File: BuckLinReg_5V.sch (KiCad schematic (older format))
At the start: 71 parts, among them J1 Barrel_Jack, J2 796638-4, J3 1x2 Male, J4 796634-4, Q1 PMBT2222, Q2 SQD40061EL, SW1 SW_SPDT, U1 TLV76050DBZT, U2 LMV358, U3 74HCT00, U4 SN74HCT02, U5 TCM810, U6 TPS56339DDC, U7 LM1084-5.0

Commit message: PCB Ordered
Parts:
- removed Q2: SQD40061EL, Package_TO_SOT_SMD:TO-252-2, symbol Device:Q_PMOS_GDS
- removed TP14: ~Q, TestPoint:TestPoint_THTPad_D2.0mm_Drill1.0mm, symbol Connector:TestPoint
- removed TP8: ~PWR_EN, TestPoint:TestPoint_THTPad_D2.0mm_Drill1.0mm, symbol Connector:TestPoint
- added Q2: Si4435FDY, Package_SO:SO-8_3.9x4.9mm_P1.27mm, symbol BuckLinReg_5V:Si4435FDY
- C2, C3: MFPN CGA5L1X7R1H106K160AE -> C3216X7R1H106K160AC
- C8, C9: MFPN CL32B106KBJNNNE -> ‎CL32B106KBJNNWE‎
- J2: MFPN (none) -> 796638-4
- J4: MFPN (none) -> 796634-4
- U7: value LM1084-5.0 -> LM1085ISX-5.0/NOPB; MFPN LM1084ISX-5.0/NOPB -> LM1085ISX-5.0/NOPB
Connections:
- net +Vin: now also C9.1, Q2.1 (S), Q2.2 (S), Q2.3 (S); no longer C3.1
- net PCheckG: now also Q2.4 (G)
- net SR+: now also C3.1; no longer C9.1
- net Vin: now also Q2.5 (D), Q2.6 (D), Q2.7 (D), Q2.8 (D)
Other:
- moved on the sheet: C3, C9
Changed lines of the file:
@@
 	9225 4150 9425 4150
-Wire Wire Line
-	3275 4825 3200 4825
 Wire Wire Line
 	3575 4825 3625 4825
@@
 Wire Wire Line
 	8000 7825 7950 7825
-Wire Wire Line
-	8000 7350 8000 7650
 Wire Wire Line
 	7950 7350 8000 7350
@@
 $EndComp
 $Comp
-L Device:Q_PMOS_GDS Q2
-U 1 1 602222D6
-P 5875 2050
-F 0 "Q2" V 6217 2050 50  0000 C CNN
-F 1 "SQD40061EL" V 6126 2050 50  0000 C CNN
-F 2 "Package_TO_SOT_SMD:TO-252-2" H 6075 2150 50  0001 C CNN
-F 3 "~" H 5875 2050 50  0001 C CNN
-F 4 "SQD40061EL" H 5875 2050 50  0001 C CNN "MFPN"
-	1    5875 2050
-	0    -1   -1   0
-$EndComp
-$Comp
 L Connector:Barrel_Jack J1
 U 1 1 602194BD
@@
 L Device:C_Small C9
 U 1 1 601E51F0
-P 8350 4400
-F 0 "C9" H 8442 4446 50  0000 L CNN
-F 1 "10u" H 8442 4355 50  0000 L CNN
-F 2 "Capacitor_SMD:C_1210_3225Metric_Pad1.33x2.70mm_HandSolder" H 8350 4400 50  0001 C CNN
-F 3 "~" H 8350 4400 50  0001 C CNN
-F 4 "CL32B106KBJNNNE" H 8350 4400 50  0001 C CNN "MFPN"
-	1    8350 4400
+P 2075 4400
+F 0 "C9" H 2167 4446 50  0000 L CNN
+F 1 "10u" H 2167 4355 50  0000 L CNN
+F 2 "Capacitor_SMD:C_1210_3225Metric_Pad1.33x2.70mm_HandSolder" H 2075 4400 50  0001 C CNN
+F 3 "~" H 2075 4400 50  0001 C CNN
+F 4 "‎CL32B106KBJNNWE‎" H 2075 4400 50  0001 C CNN "MFPN"
+	1    2075 4400
 	1    0    0    -1
 $EndComp
@@
 F 2 "Capacitor_SMD:C_1210_3225Metric_Pad1.33x2.70mm_HandSolder" H 8025 4400 50  0001 C CNN
 F 3 "~" H 8025 4400 50  0001 C CNN
-F 4 "CL32B106KBJNNNE" H 8025 4400 50  0001 C CNN "MFPN"
+F 4 "‎CL32B106KBJNNWE‎" H 8025 4400 50  0001 C CNN "MFPN"
 	1    8025 4400
 	1    0    0    -1
@@
 L Device:C_Small C3
 U 1 1 601DCCF3
-P 2075 4400
-F 0 "C3" H 2167 4446 50  0000 L CNN
-F 1 "10u" H 2167 4355 50  0000 L CNN
-F 2 "Capacitor_SMD:C_1206_3216Metric_Pad1.33x1.80mm_HandSolder" H 2075 4400 50  0001 C CNN
-F 3 "~" H 2075 4400 50  0001 C CNN
-F 4 "CGA5L1X7R1H106K160AE" H 2075 4400 50  0001 C CNN "MFPN"
-	1    2075 4400
+P 8350 4400
+F 0 "C3" H 8442 4446 50  0000 L CNN
+F 1 "10u" H 8442 4355 50  0000 L CNN
+F 2 "Capacitor_SMD:C_1206_3216Metric_Pad1.33x1.80mm_HandSolder" H 8350 4400 50  0001 C CNN
+F 3 "~" H 8350 4400 50  0001 C CNN
+F 4 "C3216X7R1H106K160AC" H 8350 4400 50  0001 C CNN "MFPN"
+	1    8350 4400
 	1    0    0    -1
 $EndComp
@@
 F 2 "Capacitor_SMD:C_1206_3216Metric_Pad1.33x1.80mm_HandSolder" H 1750 4400 50  0001 C CNN
 F 3 "~" H 1750 4400 50  0001 C CNN
-F 4 "CGA5L1X7R1H106K160AE" H 1750 4400 50  0001 C CNN "MFPN"
+F 4 "C3216X7R1H106K160AC" H 1750 4400 50  0001 C CNN "MFPN"
 	1    1750 4400
 	1    0    0    -1
@@
 P 10500 4150
 F 0 "U7" H 10500 4392 50  0000 C CNN
-F 1 "LM1084-5.0" H 10500 4301 50  0000 C CNN
+F 1 "LM1085ISX-5.0/NOPB" H 10500 4301 50  0000 C CNN
 F 2 "Package_TO_SOT_SMD:TO-263-3_TabPin2" H 10500 4400 50  0001 C CIN
 F 3 "http://www.ti.com/general/docs/suppproductinfo.tsp?distId=10&gotoUrl=http%3A%2F%2Fwww.ti.com%2Flit%2Fgpn%2Flm1084" H 10500 4150 50  0001 C CNN
-F 4 "LM1084ISX-5.0/NOPB" H 10500 4150 50  0001 C CNN "MFPN"
+F 4 "LM1085ISX-5.0/NOPB" H 10500 4150 50  0001 C CNN "MFPN"
 	1    10500 4150
 	1    0    0    -1
@@
 Connection ~ 7375 8875
 $Comp
-L Connector:TestPoint TP14
-U 1 1 604CB1A8
-P 8050 7650
-F 0 "TP14" H 8108 7768 50  0000 L CNN
-F 1 "~Q" H 8108 7677 50  0000 L CNN
-F 2 "TestPoint:TestPoint_THTPad_D2.0mm_Drill1.0mm" H 8250 7650 50  0001 C CNN
-F 3 "~" H 8250 7650 50  0001 C CNN
-	1    8050 7650
-	0    1    -1   0
-$EndComp
-Wire Wire Line
-	8050 7650 8000 7650
-Connection ~ 8000 7650
-Wire Wire Line
-	8000 7650 8000 7825
-$Comp
 L Connector:TestPoint TP12
 U 1 1 604EEC3C
@@
 	7300 7250 7300 7150
 $Comp
-L Connector:TestPoint TP8
-U 1 1 605351DA
-P 3200 4700
-F 0 "TP8" H 3258 4818 50  0000 L CNN
-F 1 "~PWR_EN" H 3258 4727 50  0000 L CNN
-F 2 "TestPoint:TestPoint_THTPad_D2.0mm_Drill1.0mm" H 3400 4700 50  0001 C CNN
-F 3 "~" H 3400 4700 50  0001 C CNN
-	1    3200 4700
-	-1   0    0    -1
-$EndComp
-Wire Wire Line
-	3200 4700 3200 4825
-Connection ~ 3200 4825
-Wire Wire Line
-	3200 4825 3125 4825
-$Comp
 L Connector:TestPoint TP15
 U 1 1 6056A5D9
@@
 F 2 "BuckLinReg_5V:796636-4" H 11500 4150 50  0001 C CNN
 F 3 "~" H 11500 4150 50  0001 C CNN
+F 4 "796638-4" H 11500 4150 50  0001 C CNN "MFPN"
 	1    11500 4150
 	1    0    0    -1
@@
 F 2 "" H 12275 4150 50  0001 C CNN
 F 3 "~" H 12275 4150 50  0001 C CNN
+F 4 "796634-4" H 12275 4150 50  0001 C CNN "MFPN"
 	1    12275 4150
 	1    0    0    -1
@@
 Text Notes 12500 4125 0    50   ~ 0
 Included to be present\non the BOM table
+Wire Wire Line
+	3125 4825 3275 4825
+Wire Wire Line
+	8000 7350 8000 7825
+$Comp
+L BuckLinReg_5V:Si4435FDY Q2
+U 1 1 6059001A
+P 5875 2000
+F 0 "Q2" V 6167 2000 50  0000 C CNN
+F 1 "Si4435FDY" V 6076 2000 50  0000 C CNN
+F 2 "Package_SO:SO-8_3.9x4.9mm_P1.27mm" H 5875 2450 50  0001 C CNN
+F 3 "" H 5875 2450 50  0001 C CNN
+	1    5875 2000
+	0    -1   -1   0
+$EndComp
 $EndSCHEMATC

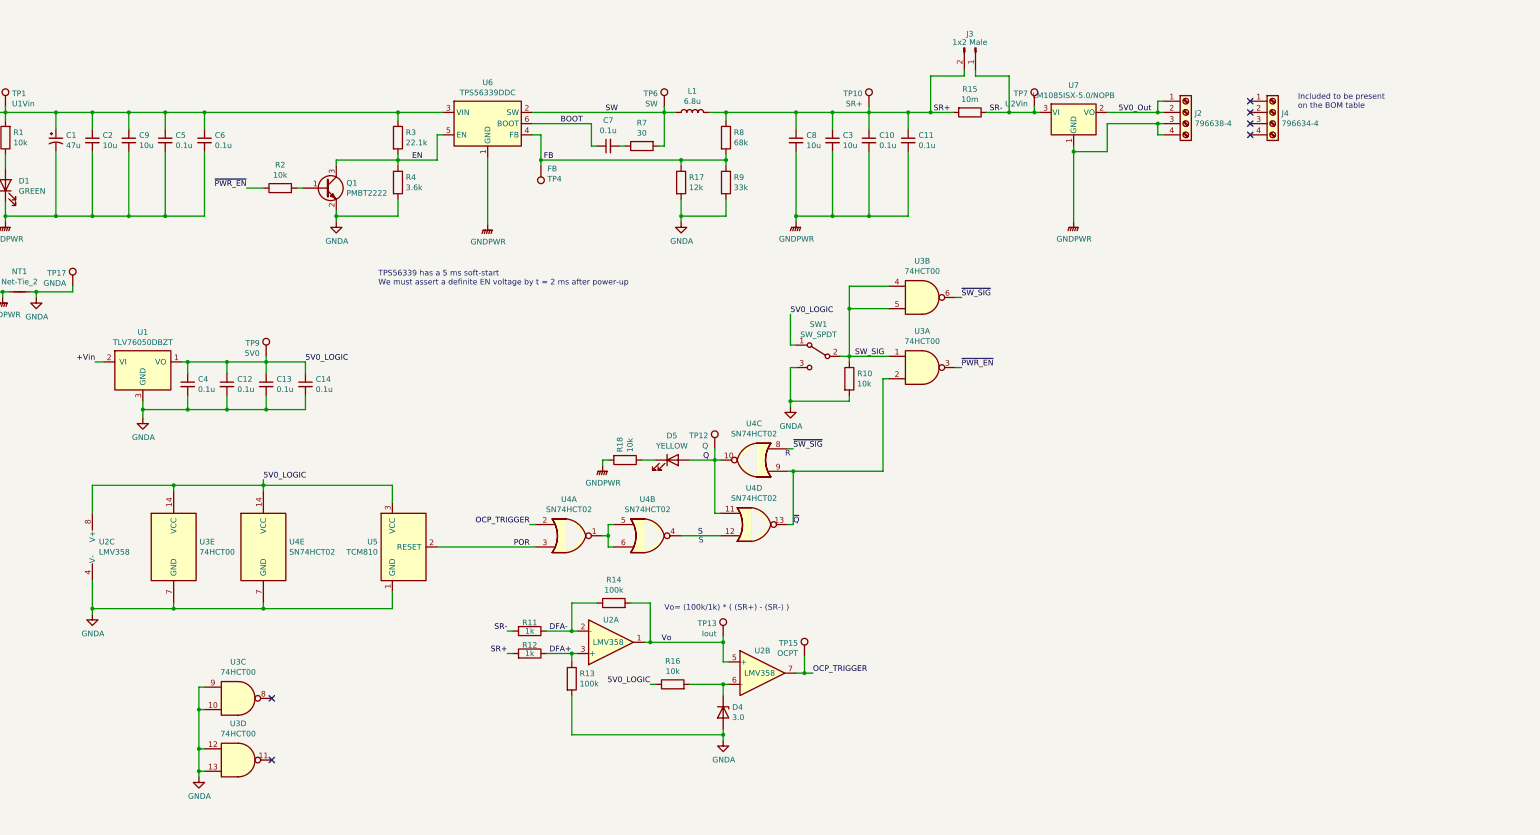
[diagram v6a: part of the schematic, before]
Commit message: Begin rev. 2 sch and PCB resize to 94x54mm
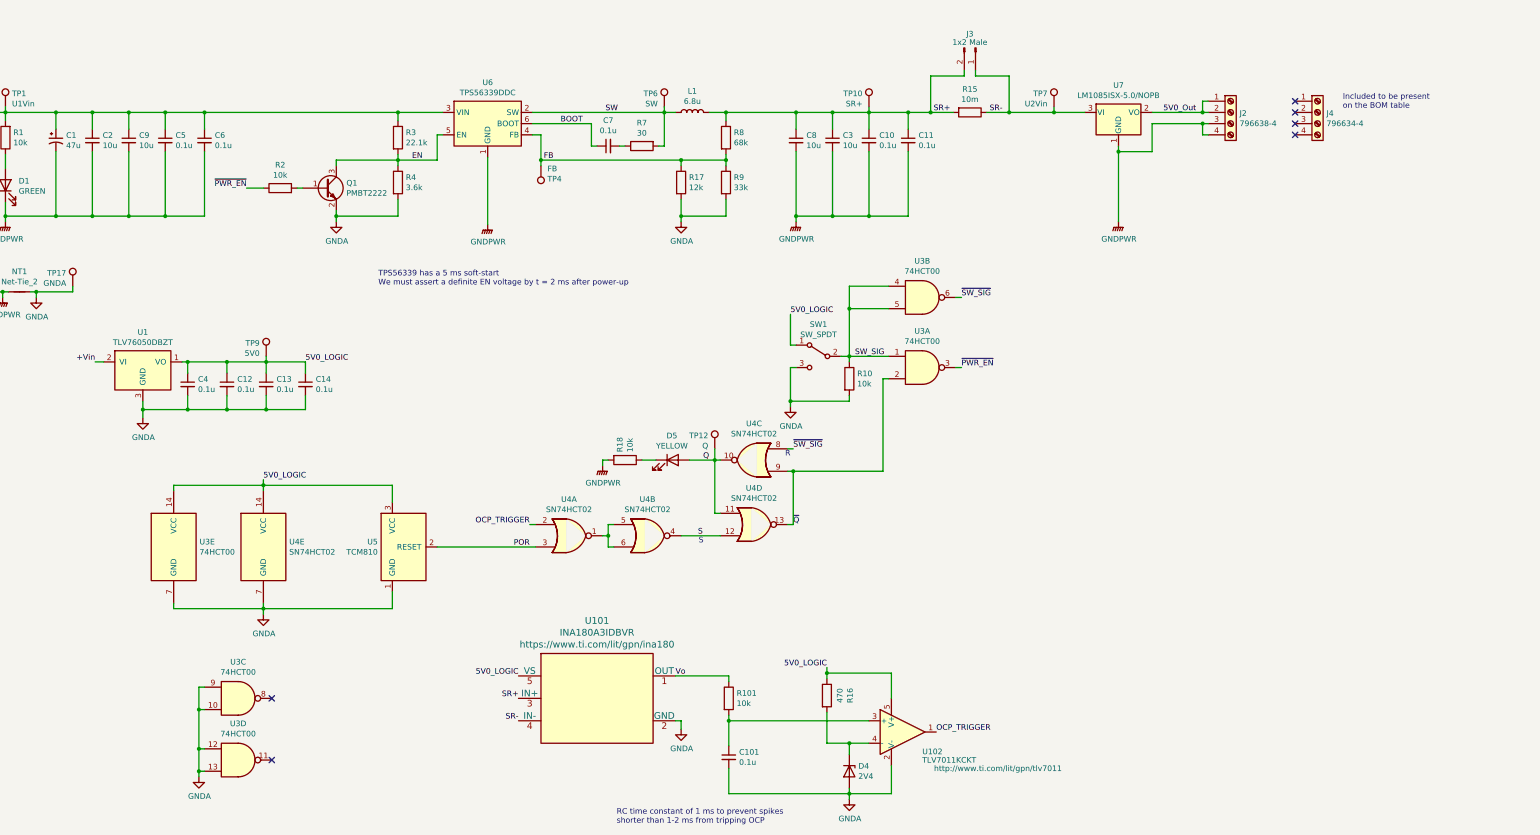
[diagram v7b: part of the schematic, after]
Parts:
- removed R11, R12: 1k, Resistor_SMD:R_1206_3216Metric_Pad1.30x1.75mm_HandSolder, symbol Device:R
- removed R13, R14: 100k, Resistor_SMD:R_1206_3216Metric_Pad1.30x1.75mm_HandSolder, symbol Device:R
- removed TP13: Iout, TestPoint:TestPoint_THTPad_D2.0mm_Drill1.0mm, symbol Connector:TestPoint
- removed TP15: OCPT, TestPoint:TestPoint_THTPad_D2.0mm_Drill1.0mm, symbol Connector:TestPoint
- removed U2: LMV358, Package_SO:SOIC-8_3.9x4.9mm_P1.27mm, symbol Amplifier_Operational:LMV358
- added C101: 0.1u, Capacitor_SMD:C_0603_1608Metric_Pad1.08x0.95mm_HandSolder, symbol Device:C_Small
- added R101: 10k, Resistor_SMD:R_1206_3216Metric_Pad1.30x1.75mm_HandSolder, symbol Device:R
- added U101: INA180A3IDBVR, Package_TO_SOT_SMD:SOT-23-5_HandSoldering, symbol BuckLinReg_5V:INA180A3IDBVR
- added U102: TLV7011KCKT, Package_TO_SOT_SMD:SOT-23-5_HandSoldering, symbol Comparator:TLV7031DBV
- D4: value 3.0 -> 2V4; footprint Diode_SMD:D_SOD-323 -> Package_TO_SOT_SMD:SOT-23_Handsoldering; MFPN PDZ3.0B,115 -> BZX84-C2V4,215
- R16: value 10k -> 470
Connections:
- net 5V0_LOGIC: now also U101.5 (VS), U102.5 (V+)
- net GNDA: now also C101.2, U101.2 (GND), U102.2 (V-)
- net OCP_TRIGGER: now also U102.1
- net SR+: now also U101.3 (IN+)
- net SR-: now also U101.4 (IN-)
- net Vo: now also R101.1, U101.1 (OUT)
- net at D4.1 (K), R16.2: now also U102.4 (-)
- new net: C101.1, R101.2, U102.3 (+)
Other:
- note added: "RC time constant of 1 ms to prevent spikes\nshorter than 1-2 ms from tripping OCP"
- note removed: "Vo= (100k/1k) * ( (SR+) - (SR-) )"
- moved on the sheet: D4, J2, J4, R16, TP7, U7

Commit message: Completed initial layout of rev. 2
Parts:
- D4: footprint Package_TO_SOT_SMD:SOT-23_Handsoldering -> Diode_SMD:D_SOD-323_HandSoldering; MFPN BZX84-C2V4,215 -> PDZ2.4B,115
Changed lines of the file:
@@
 F 0 "D4" V 8454 10105 50  0000 L CNN
 F 1 "2V4" V 8545 10105 50  0000 L CNN
-F 2 "Package_TO_SOT_SMD:SOT-23_Handsoldering" H 8500 10025 50  0001 C CNN
-F 3 "https://rocelec.widen.net/view/pdf/fysgtbvgew/PHGLS29437-1.pdf?t.download=true&u=5oefqw" H 8500 10025 50  0001 C CNN
-F 4 "BZX84-C2V4,215" V 8500 10025 50  0001 C CNN "MFPN"
+F 2 "Diode_SMD:D_SOD-323_HandSoldering" H 8500 10025 50  0001 C CNN
+F 3 "https://rocelec.widen.net/view/pdf/girsb18scs/PHGLS19616-1.pdf?t.download=true&u=5oefqw" H 8500 10025 50  0001 C CNN
+F 4 "PDZ2.4B,115" V 8500 10025 50  0001 C CNN "MFPN"
 	1    8500 10025
 	0    1    1    0
